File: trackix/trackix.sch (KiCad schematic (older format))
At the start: 78 parts, among them IC2 TP4056, J1 BATTERY, J2 GPS, J3 Conn_01x05_Male, J4 AVR-ISP-6, J5 Conn_01x05_Male, Q1 2N3904, Q3 FS8205A, Q5 2N3904, U1 ATmega328P-AU, U2 SIM28ML, U3 DW-01, U4 TPS62291DRVR

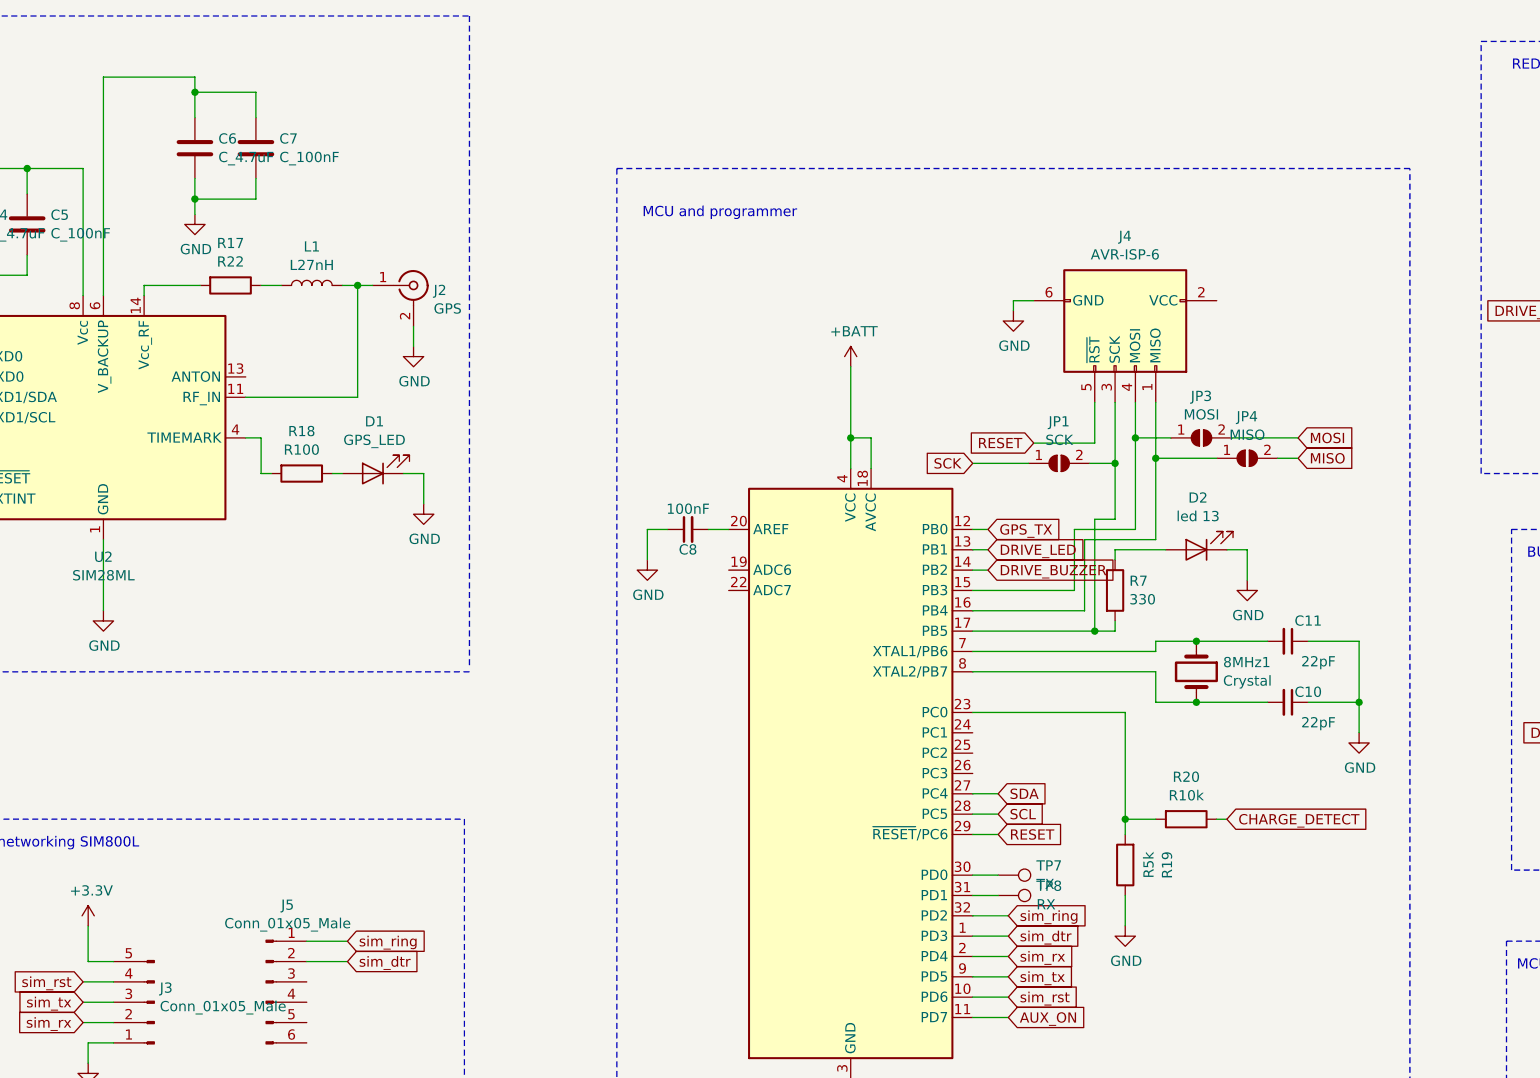
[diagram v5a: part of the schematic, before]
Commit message: added gsm version
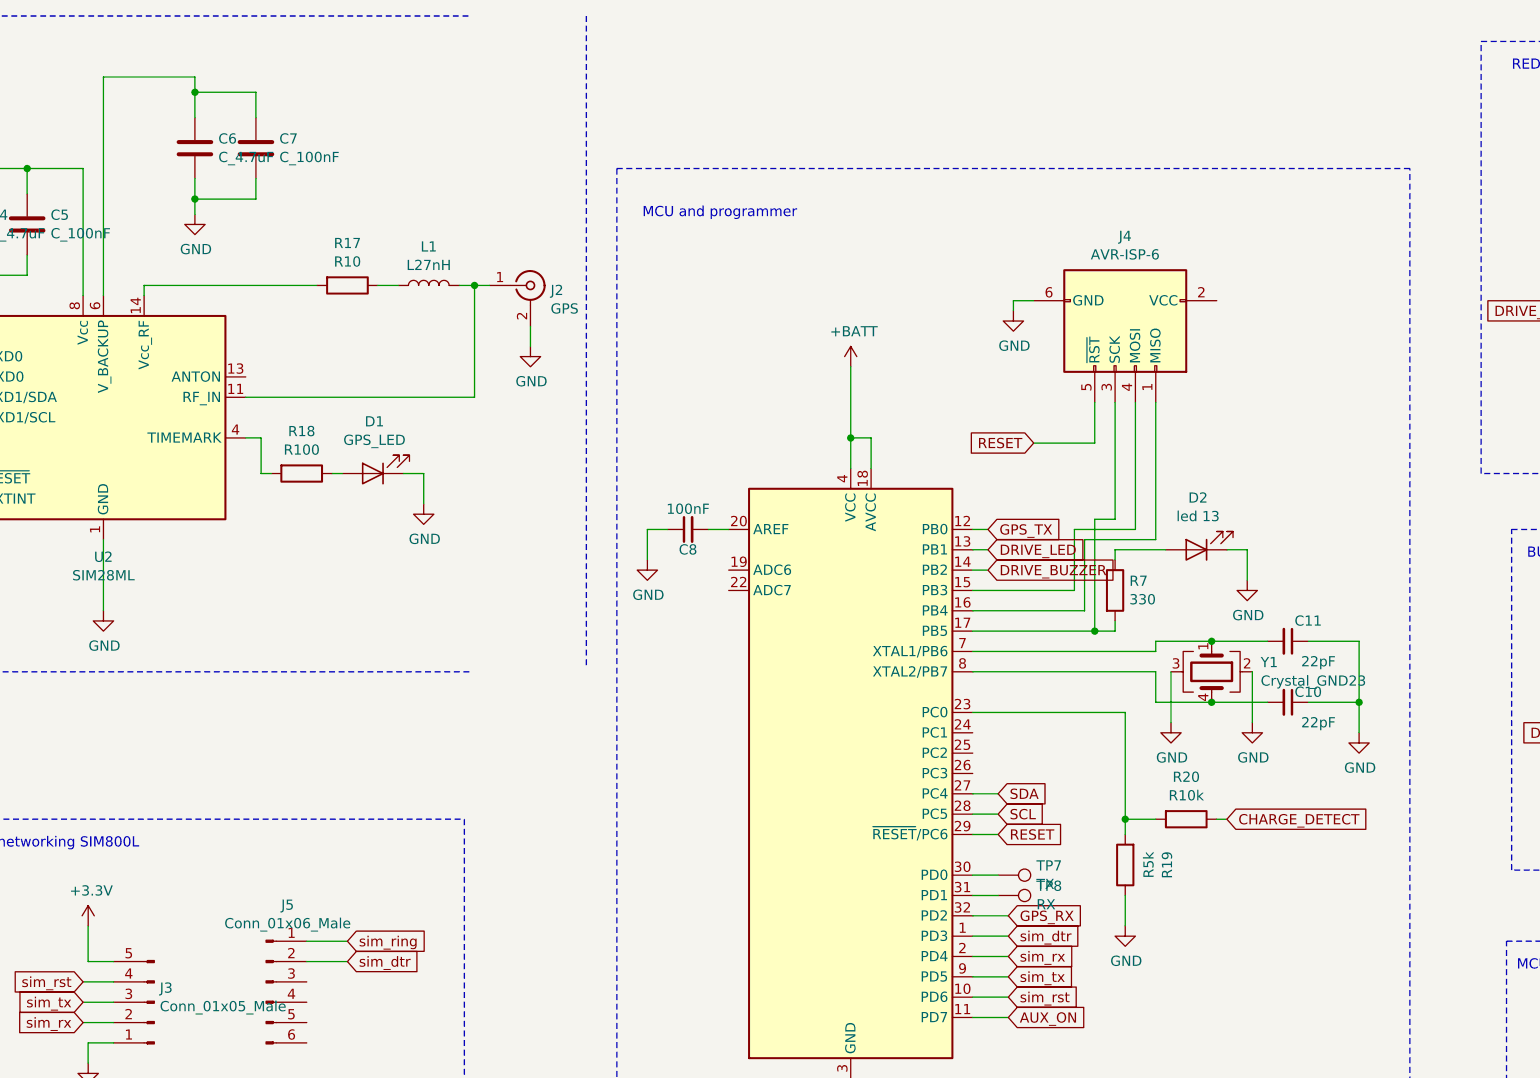
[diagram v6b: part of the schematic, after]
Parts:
- removed 8MHz1: Crystal, Crystals:Crystal_SMD_3225-4pin_3.2x2.5mm_HandSoldering, symbol trackix-rescue:Crystal-Device-trackix-rescue
- removed JP1: SCK, Jumper:SolderJumper-2_P1.3mm_Open_RoundedPad1.0x1.5mm, symbol Jumper:SolderJumper_2_Open
- removed JP3: MOSI, Jumper:SolderJumper-2_P1.3mm_Open_RoundedPad1.0x1.5mm, symbol Jumper:SolderJumper_2_Open
- removed JP4: MISO, Jumper:SolderJumper-2_P1.3mm_Open_RoundedPad1.0x1.5mm, symbol Jumper:SolderJumper_2_Open
- added Y1: Crystal_GND23, Crystals:Crystal_SMD_3225-4pin_3.2x2.5mm_HandSoldering, symbol Device:Crystal_GND23
- J5: value Conn_01x05_Male -> Conn_01x06_Male; footprint Pin_Headers:Pin_Header_Straight_1x05_Pitch2.54mm -> Pin_Headers:Pin_Header_Straight_1x06_Pitch2.54mm
- R17: value R22 -> R10
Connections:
- net GND: now also Y1.2, Y1.3
- net GPS_RX: now also U1.32 (PD2)
- net sim_ring: no longer U1.32 (PD2)
- net at C11.2, U1.7 (XTAL1/PB6): now also Y1.1
- net at C10.2, U1.8 (XTAL2/PB7): now also Y1.4
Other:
- moved on the sheet: J2, L1, R17
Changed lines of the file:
@@
 $EndDescr
-$Comp
-L trackix-rescue:Crystal-Device-trackix-rescue 8MHz1
-U 1 1 5C69FEF1
-P 11125 4525
-F 0 "8MHz1" V 11079 4656 50  0000 L CNN
-F 1 "Crystal" V 11170 4656 50  0000 L CNN
-F 2 "Crystals:Crystal_SMD_3225-4pin_3.2x2.5mm_HandSoldering" H 11125 4525 50  0001 C CNN
-F 3 "~" H 11125 4525 50  0001 C CNN
-	1    11125 4525
-	0    1    1    0
-$EndComp
 $Comp
 L trackix-rescue:C_Small-Device-trackix-rescue C11
@@
 	0    1    1    0
 $EndComp
-Wire Wire Line
-	11125 4675 11475 4675
-Wire Wire Line
-	11125 4375 11475 4375
 $Comp
 L power:GND #PWR0110
@@
 	10925 4525 10925 4675
 Wire Wire Line
-	10925 4675 11125 4675
-Connection ~ 11125 4675
-Wire Wire Line
 	10025 4425 10925 4425
 Wire Wire Line
 	10925 4425 10925 4375
-Wire Wire Line
-	10925 4375 11125 4375
-Connection ~ 11125 4375
 $Comp
 L power:GND #PWR0111
@@
 	10625 4325 10725 4325
 Wire Wire Line
-	10925 3200 10925 3475
-Wire Wire Line
 	10925 3875 10575 3875
 Wire Wire Line
@@
 Wire Wire Line
 	10575 4225 10025 4225
-Wire Wire Line
-	10825 3200 10825 3375
 Wire Wire Line
 	10825 3825 10525 3825
@@
 $EndComp
 $Comp
-L trackix-rescue:ATmega328P-AU-MCU_Microchip_ATmega-trackix-rescue U1
-U 1 1 5C69F59F
-P 9425 5025
-F 0 "U1" H 9425 3439 50  0000 C CNN
-F 1 "ATmega328P-AU" H 9425 3348 50  0000 C CNN
-F 2 "Housings_QFP:TQFP-32_7x7mm_Pitch0.8mm" H 9425 5025 50  0001 C CIN
-F 3 "http://ww1.microchip.com/downloads/en/DeviceDoc/ATmega328_P%20AVR%20MCU%20with%20picoPower%20Technology%20Data%20Sheet%2040001984A.pdf" H 9425 5025 50  0001 C CNN
-	1    9425 5025
-	1    0    0    -1
-$EndComp
-$Comp
 L trackix-rescue:AVR-ISP-6-Connector-trackix-rescue J4
 U 1 1 5C6CC941
@@
 L trackix-rescue:Conn_Coaxial-Connector-trackix-rescue J2
 U 1 1 5E9805A1
-P 7275 2625
-F 0 "J2" H 7374 2601 50  0000 L CNN
-F 1 "GPS" H 7374 2510 50  0000 L CNN
-F 2 "Connectors_Molex:Molex_Microcoaxial_RF" H 7275 2625 50  0001 C CNN
-F 3 "" H 7275 2625 50  0001 C CNN
-	1    7275 2625
+P 7850 2625
+F 0 "J2" H 7949 2601 50  0000 L CNN
+F 1 "GPS" H 7949 2510 50  0000 L CNN
+F 2 "Connectors_Molex:Molex_Microcoaxial_RF" H 7850 2625 50  0001 C CNN
+F 3 "" H 7850 2625 50  0001 C CNN
+	1    7850 2625
 	1    0    0    -1
 $EndComp
@@
 L power:GND #PWR0135
 U 1 1 5E9806DC
-P 7275 2925
-F 0 "#PWR0135" H 7275 2675 50  0001 C CNN
-F 1 "GND" H 7280 2752 50  0000 C CNN
-F 2 "" H 7275 2925 50  0001 C CNN
-F 3 "" H 7275 2925 50  0001 C CNN
-	1    7275 2925
-	1    0    0    -1
-$EndComp
-Wire Wire Line
-	7275 2825 7275 2925
+P 7850 2925
+F 0 "#PWR0135" H 7850 2675 50  0001 C CNN
+F 1 "GND" H 7855 2752 50  0000 C CNN
+F 2 "" H 7850 2925 50  0001 C CNN
+F 3 "" H 7850 2925 50  0001 C CNN
+	1    7850 2925
+	1    0    0    -1
+$EndComp
+Wire Wire Line
+	7850 2825 7850 2925
 $Comp
 L Device:C C6
@@
 L Device:L L1
 U 1 1 5ECC283D
-P 6775 2625
-F 0 "L1" V 6965 2625 50  0000 C CNN
-F 1 "L27nH" V 6874 2625 50  0000 C CNN
-F 2 "Inductors_SMD:L_0402" H 6775 2625 50  0001 C CNN
-F 3 "~" H 6775 2625 50  0001 C CNN
-	1    6775 2625
+P 7350 2625
+F 0 "L1" V 7540 2625 50  0000 C CNN
+F 1 "L27nH" V 7449 2625 50  0000 C CNN
+F 2 "Inductors_SMD:L_0402" H 7350 2625 50  0001 C CNN
+F 3 "~" H 7350 2625 50  0001 C CNN
+	1    7350 2625
 	0    -1   -1   0
 $EndComp
@@
 L device:R R17
 U 1 1 5ECC2D77
-P 6375 2625
-F 0 "R17" V 6168 2625 50  0000 C CNN
-F 1 "R22" V 6259 2625 50  0000 C CNN
-F 2 "Resistors_SMD:R_0805" V 6305 2625 50  0001 C CNN
-F 3 "~" H 6375 2625 50  0001 C CNN
-	1    6375 2625
+P 6950 2625
+F 0 "R17" V 6743 2625 50  0000 C CNN
+F 1 "R10" V 6834 2625 50  0000 C CNN
+F 2 "Resistors_SMD:R_0805" V 6880 2625 50  0001 C CNN
+F 3 "~" H 6950 2625 50  0001 C CNN
+	1    6950 2625
 	0    1    1    0
 $EndComp
 Wire Wire Line
-	6525 2625 6625 2625
-Wire Wire Line
-	6925 2625 7000 2625
+	7100 2625 7200 2625
+Wire Wire Line
+	7500 2625 7575 2625
 Wire Wire Line
 	6200 1600 5750 1600
@@
 	5750 1600 5750 2675
 Wire Wire Line
-	7000 2625 7000 3175
-Wire Wire Line
-	6450 3175 7000 3175
-Connection ~ 7000 2625
-Wire Wire Line
-	7000 2625 7075 2625
-Wire Wire Line
-	6225 2625 5950 2625
+	7575 2625 7575 3175
+Connection ~ 7575 2625
+Wire Wire Line
+	7575 2625 7650 2625
 Wire Wire Line
 	5950 2625 5950 2675
@@
 Wire Wire Line
 	10025 3925 10100 3925
-Text GLabel 10025 3500 0    50   Input ~ 0
-SCK
-Text GLabel 11625 3375 2    50   Input ~ 0
-MOSI
-Wire Wire Line
-	10825 3375 11000 3375
-Wire Wire Line
-	10725 3200 10725 3500
-Connection ~ 10825 3375
-Wire Wire Line
-	10825 3375 10825 3825
-Text GLabel 11625 3475 2    50   Input ~ 0
-MISO
-Wire Wire Line
-	11225 3475 10925 3475
-Connection ~ 10925 3475
-Wire Wire Line
-	10925 3475 10925 3875
 Wire Wire Line
 	10025 6125 10200 6125
@@
 Text GLabel 13150 6775 0    50   Input ~ 0
 RESET
-Connection ~ 10725 3500
-Wire Wire Line
-	10725 3500 10725 3775
 Text GLabel 10150 5125 2    50   Input ~ 0
 SDA
@@
 Wire Wire Line
 	1800 10075 1875 10075
-$Comp
-L Jumper:SolderJumper_2_Open JP3
-U 1 1 5E888631
-P 11150 3375
-F 0 "JP3" H 11150 3580 50  0000 C CNN
-F 1 "MOSI" H 11150 3489 50  0000 C CNN
-F 2 "Jumper:SolderJumper-2_P1.3mm_Open_RoundedPad1.0x1.5mm" H 11150 3375 50  0001 C CNN
-F 3 "~" H 11150 3375 50  0001 C CNN
-	1    11150 3375
-	1    0    0    -1
-$EndComp
-$Comp
-L Jumper:SolderJumper_2_Open JP4
-U 1 1 5E888BC3
-P 11375 3475
-F 0 "JP4" H 11375 3680 50  0000 C CNN
-F 1 "MISO" H 11375 3589 50  0000 C CNN
-F 2 "Jumper:SolderJumper-2_P1.3mm_Open_RoundedPad1.0x1.5mm" H 11375 3475 50  0001 C CNN
-F 3 "~" H 11375 3475 50  0001 C CNN
-	1    11375 3475
-	1    0    0    -1
-$EndComp
-Wire Wire Line
-	11300 3375 11625 3375
-Wire Wire Line
-	11625 3475 11525 3475
-$Comp
-L Jumper:SolderJumper_2_Open JP1
-U 1 1 5EA34996
-P 10450 3500
-F 0 "JP1" H 10450 3705 50  0000 C CNN
-F 1 "SCK" H 10450 3614 50  0000 C CNN
-F 2 "Jumper:SolderJumper-2_P1.3mm_Open_RoundedPad1.0x1.5mm" H 10450 3500 50  0001 C CNN
-F 3 "~" H 10450 3500 50  0001 C CNN
-	1    10450 3500
-	1    0    0    -1
-$EndComp
-Wire Wire Line
-	10025 3500 10300 3500
-Wire Wire Line
-	10600 3500 10725 3500
 Wire Wire Line
 	10325 3400 10625 3400
@@
 	3975 1300 7550 1300
 Wire Notes Line
-	7550 1300 7550 4500
+	8125 1300 8125 4500
 Text Notes 11425 7800 0    50   ~ 0
 3.3v Regulator\n
@@
 P 6550 6050
 F 0 "J5" H 6656 6428 50  0000 C CNN
-F 1 "Conn_01x05_Male" H 6656 6337 50  0000 C CNN
-F 2 "Pin_Headers:Pin_Header_Straight_1x05_Pitch2.54mm" H 6550 6050 50  0001 C CNN
+F 1 "Conn_01x06_Male" H 6656 6337 50  0000 C CNN
+F 2 "Pin_Headers:Pin_Header_Straight_1x06_Pitch2.54mm" H 6550 6050 50  0001 C CNN
 F 3 "~" H 6550 6050 50  0001 C CNN
 	1    6550 6050
@@
 Text GLabel 10200 5925 2    50   Input ~ 0
 sim_rx
-Text GLabel 10200 5725 2    50   Input ~ 0
-sim_ring
 Text GLabel 10200 5825 2    50   Input ~ 0
 sim_dtr
@@
 	1    0    0    -1
 $EndComp
+Wire Wire Line
+	10925 3200 10925 3875
+Wire Wire Line
+	10825 3200 10825 3825
+$Comp
+L trackix-rescue:ATmega328P-AU-MCU_Microchip_ATmega-trackix-rescue U1
+U 1 1 5C69F59F
+P 9425 5025
+F 0 "U1" H 9425 3439 50  0000 C CNN
+F 1 "ATmega328P-AU" H 9425 3348 50  0000 C CNN
+F 2 "Housings_QFP:TQFP-32_7x7mm_Pitch0.8mm" H 9425 5025 50  0001 C CIN
+F 3 "http://ww1.microchip.com/downloads/en/DeviceDoc/ATmega328_P%20AVR%20MCU%20with%20picoPower%20Technology%20Data%20Sheet%2040001984A.pdf" H 9425 5025 50  0001 C CNN
+	1    9425 5025
+	1    0    0    -1
+$EndComp
+Wire Wire Line
+	10725 3200 10725 3775
+Text GLabel 10200 5725 2    50   Input ~ 0
+GPS_RX
+$Comp
+L Device:Crystal_GND23 Y1
+U 1 1 5F64A711
+P 11200 4525
+F 0 "Y1" V 11154 4766 50  0000 L CNN
+F 1 "Crystal_GND23" V 11245 4766 50  0000 L CNN
+F 2 "Crystals:Crystal_SMD_3225-4pin_3.2x2.5mm_HandSoldering" H 11200 4525 50  0001 C CNN
+F 3 "~" H 11200 4525 50  0001 C CNN
+	1    11200 4525
+	0    1    1    0
+$EndComp
+Wire Wire Line
+	10925 4375 11200 4375
+Wire Wire Line
+	10925 4675 11200 4675
+Connection ~ 11200 4375
+Connection ~ 11200 4675
+Wire Wire Line
+	11200 4375 11475 4375
+Wire Wire Line
+	11200 4675 11475 4675
+$Comp
+L power:GND #PWR0144
+U 1 1 5F688FB9
+P 11400 4775
+F 0 "#PWR0144" H 11400 4525 50  0001 C CNN
+F 1 "GND" H 11405 4602 50  0000 C CNN
+F 2 "" H 11400 4775 50  0001 C CNN
+F 3 "" H 11400 4775 50  0001 C CNN
+	1    11400 4775
+	1    0    0    -1
+$EndComp
+$Comp
+L power:GND #PWR0146
+U 1 1 5F69DBA3
+P 11000 4775
+F 0 "#PWR0146" H 11000 4525 50  0001 C CNN
+F 1 "GND" H 11005 4602 50  0000 C CNN
+F 2 "" H 11000 4775 50  0001 C CNN
+F 3 "" H 11000 4775 50  0001 C CNN
+	1    11000 4775
+	1    0    0    -1
+$EndComp
+Wire Wire Line
+	11400 4525 11400 4775
+Wire Wire Line
+	11000 4525 11000 4775
+Wire Wire Line
+	6450 3175 7575 3175
+Wire Wire Line
+	5950 2625 6800 2625
 $EndSCHEMATC
